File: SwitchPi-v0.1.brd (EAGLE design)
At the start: 81 x 61 mm, 10 parts, among them IC1 MCP23017SP, IC2 MCP2300X/P, P2 P2, P3 P3

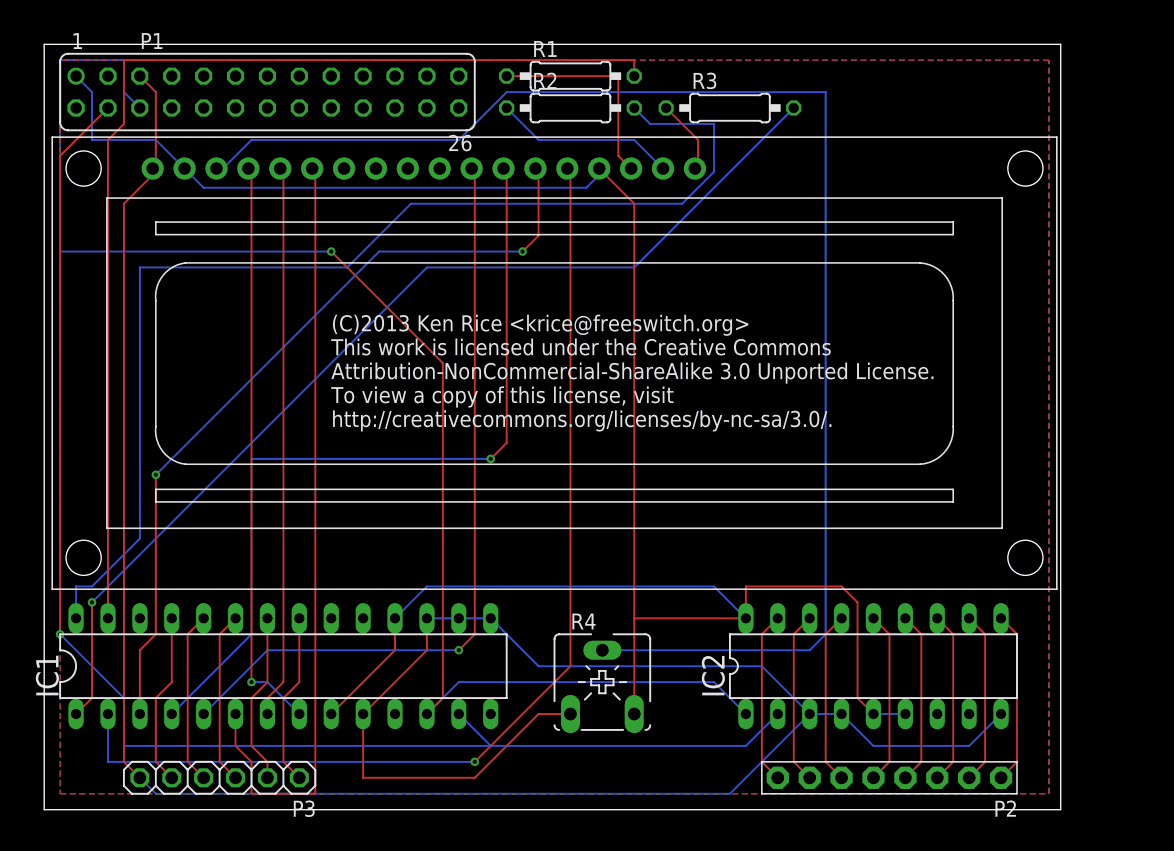
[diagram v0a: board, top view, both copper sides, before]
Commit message: small changes to board layout to clean up some traces
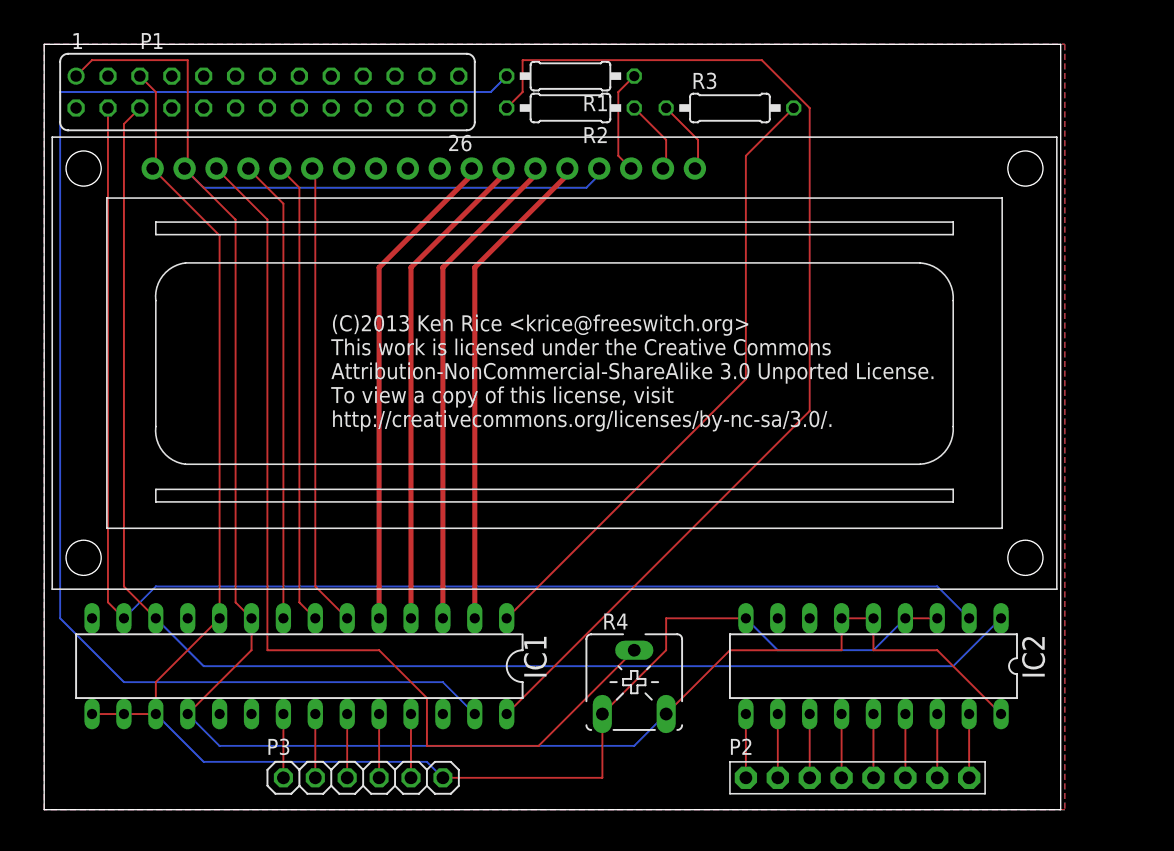
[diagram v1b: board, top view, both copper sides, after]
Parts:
- moved P3 11.4 mm to (25.4, 2.54), turned to 0 degrees
- moved P2 2.54 mm to (64.8, 2.54), turned to 0 degrees
- moved R4 2.54 mm to (47.0, 10.2)
- moved IC1 1.27 mm to (20.3, 11.4), turned to 180 degrees
- turned IC2 to 180 degrees
- turned R1 to 180 degrees
- turned R2 to 180 degrees
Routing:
- net GND: track 199.2 -> 137.1 mm
- net GPB1: track 83.5 -> 38.9 mm, vias 1 -> 0
- net N$3: track 112.7 -> 77.8 mm
- net GPB0: track 81.6 -> 50.1 mm, vias 1 -> 0
- net GPA6: track 86.9 -> 114.2 mm
- net GPB3: track 65.7 -> 38.9 mm, vias 1 -> 0
- net GPB5: track 61.8 -> 37.0 mm
- net GPB2: track 63.4 -> 38.9 mm, vias 2 -> 0
- net GPB4: track 61.4 -> 38.9 mm, vias 1 -> 0
- net +5V: track 166.2 -> 177.0 mm
- net GPB7: track 45.9 -> 37.0 mm, vias 1 -> 0
- net N$2: track 13.8 -> 5.08 mm
- net N$9: track 13.8 -> 5.08 mm
- net N$8: track 13.8 -> 5.08 mm
- net N$10: track 13.8 -> 5.08 mm
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- added copper zone on layer 16, net GND
- removed copper zone on layer 16, net GROUND
